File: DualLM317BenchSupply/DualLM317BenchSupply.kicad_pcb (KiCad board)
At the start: 2 copper layers, 39 parts, among them CON101 BARREL_JACK, P103 CONN_1, P104 CONN_1, SW101 SPDT, SW102 SPDT, SW103 SPDT, SW201 SP6T, U101 LM317, U102 LM317, U103 7805

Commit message: updating parts
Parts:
- removed C103, C105: 1uF, C1V7
- removed C104, C107: 10uF, C1V7
- C102: footprint C2V10 -> ELCAP_2_52_V
- CON101: footprint BARREL_JACK -> BARREL_JACK_21x55
- moved U103 14.5 mm to (129.5, 175.3)
- moved C102 9.16 mm to (114.3, 175.3), turned to 270 degrees
- moved CON101 1.27 mm to (101.6, 177.8)
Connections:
- C101 pad 1: N-000009 -> N-0000010
- C102 pad 1: N-000009 -> N-0000010
- C106 pad 1: N-000009 -> N-0000010
- D101 pad 1: N-000009 -> N-0000010
- D104 pad 2: N-000009 -> N-0000010
- SW101 pad 1: N-000009 -> N-0000010
- SW102 pad 2: N-000009 -> N-0000010
- SW201 pad 1: (no net) -> /current_limit_r/IN
- SW201 pad 2: (no net) -> N-0000017
- SW201 pad 3: (no net) -> N-0000016
- SW201 pad 4: (no net) -> N-0000020
- SW201 pad 5: (no net) -> N-0000021
- SW201 pad 6: (no net) -> N-0000018
- SW201 pad 7: (no net) -> N-0000022
- U101 pad 1: N-000009 -> N-0000010
- U103 pad 1: (no net) -> N-0000010
- U103 pad 2: (no net) -> GND
- U103 pad 3: (no net) -> 5V

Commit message: updating switches, capacitors, and LEDs
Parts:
- added C103: 1uF, C1V7, F.Cu at (20.3, 30.5)
- added C104: 10uF, C1V7, F.Cu at (33.0, 30.5)
- added C105: 1uF, C1V7, F.Cu at (43.2, 17.8)
- added C107: 10uF, C1V7, F.Cu at (30.5, 20.3)
- D101: footprint LED-5MM -> LED_5MM
- U101: value LM317 -> 7805
- U103: value 7805 -> LM317
- moved D101 156.2 mm to (121.9, 182.9)
- moved R101 138.5 mm to (129.5, 182.9)
- moved R103 92.4 mm to (207.0, 167.6)
- moved R201 79.3 mm to (168.9, 154.9)
- moved R202 79.3 mm to (193.0, 149.9)
- moved R203 79.3 mm to (175.3, 163.8)
- moved R205 79.3 mm to (193.0, 157.5)
- moved R206 79.3 mm to (179.1, 148.6)
- moved R207 79.3 mm to (154.9, 157.5)
- moved R210 79.3 mm to (189.2, 165.1)
- moved R212 79.3 mm to (160.0, 161.3)
- moved R204 79.3 mm to (156.2, 167.6)
- moved R208 79.3 mm to (184.2, 153.7)
- moved R209 79.3 mm to (174.0, 167.6)
- moved R211 73.9 mm to (185.4, 172.7)
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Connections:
- C101 pad 1: N-0000010 (its old number) -> N-0000015
- C102 pad 1: N-0000010 (its old number) -> N-0000015
- C106 pad 1: N-0000010 (its old number) -> N-0000015
- D101 pad 1: N-0000010 (its old number) -> N-0000015
- D102 pad 1: N-0000015 -> N-000005
- D103 pad 1: N-0000012 (its old number) -> N-0000014
- D103 pad 2: N-0000015 -> N-000005
- D104 pad 2: N-0000010 (its old number) -> N-0000015
- R103 pad 1: N-0000015 -> N-000005
- R103 pad 2: N-0000012 (its old number) -> N-0000014
- RV101 pad 3: N-0000012 (its old number) -> N-0000014
- SW101 pad 1: N-0000010 (its old number) -> N-0000015
- SW102 pad 2: N-0000010 (its old number) -> N-0000015
- SW103 pad 2: N-0000015 -> N-000005
- U101 pad 1: N-0000010 (its old number) -> N-0000015
- U101 pad 2: /current_limit_r/OUT -> GND
- U101 pad 3: /current_limit_r/IN -> 5V
- U102 pad 1: N-0000013 -> /current_limit_r/OUT
- U102 pad 2: N-0000012 (its old number) -> /current_limit_r/IN
- U103 pad 1: N-0000010 (its old number) -> N-0000014
- U103 pad 2: GND -> N-000005
- U103 pad 3: 5V -> N-0000013

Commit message: moving status LED to 5V rail.  starting initial layout.
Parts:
- added D1: 1N4148, D3, F.Cu at (170.2, 188.0)
- C102: value 1000uF -> 100uF
- R101: value 1k -> 150
- R201, R202, R203, R204, R205, R206, R207, R208, R209, R210, R211, R212: footprint R_AXIAL_0W25 -> R1
- moved C105 179.5 mm to (119.4, 180.3)
- moved C103 177.7 mm to (111.8, 182.9)
- moved C107 164.7 mm to (104.1, 167.6)
- moved C104 150.9 mm to (121.9, 152.4)
- moved C106 142.8 mm to (99.1, 154.9)
- moved SW201 141.2 mm to (157.5, 185.4), turned to 180 degrees
- moved C101 140.6 mm to (99.1, 149.9)
- moved SW103 130.3 mm to (127.0, 165.1)
- moved D103 126.2 mm to (109.2, 142.2)
- moved SW101 118.8 mm to (167.6, 157.5), turned to 90 degrees
- moved D104 118.7 mm to (114.3, 124.5)
- moved SW102 112.2 mm to (167.6, 167.6), turned to 90 degrees
- moved D102 106.1 mm to (137.2, 167.6)
- moved RV101 101.8 mm to (167.6, 147.3), turned to 90 degrees
- moved R103 80.0 mm to (127.0, 167.6), turned to 180 degrees
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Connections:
- C101 pad 1: N-0000015 (its old number) -> N-000008
- C102 pad 1: N-0000015 (its old number) -> N-000008
- C104 pad 1: N-0000014 (its old number) -> N-000006
- C106 pad 1: N-0000015 (its old number) -> N-000008
- D101 pad 1: N-0000015 (its old number) -> 5V
- D103 pad 1: N-0000014 (its old number) -> N-000006
- D104 pad 2: N-0000015 (its old number) -> N-000008
- R103 pad 2: N-0000014 (its old number) -> N-000006
- RV101 pad 2: GND -> N-000006
- RV101 pad 3: N-0000014 (its old number) -> N-000006
- SW101 pad 1: N-0000015 (its old number) -> N-000008
- SW102 pad 2: N-0000015 (its old number) -> N-000008
- U101 pad 1: N-0000015 (its old number) -> N-000008
- U102 pad 3: N-0000015 (its old number) -> N-000008
- U103 pad 1: N-0000014 (its old number) -> N-000006
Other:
- board outline added: 81.3 x 68.6 mm

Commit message: working on board layout
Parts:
- removed C101, C106: 0.1uF, C2
- removed C102: 100uF, ELCAP_2_52_V
- removed C103, C105: 1uF, C1V7
- removed C104, C107: 10uF, C1V7
- removed CON101: BARREL_JACK, BARREL_JACK_21x55
- removed D1, D102, D103, D104: 1N4148, D3
- removed D101: LED, LED_5MM
- removed DS101: AMMETER, PIN_ARRAY_4x1
- removed DS102: VOLTMETER, PIN_ARRAY_3X1
- removed the H*** at (124.5, 133.3)
- removed P103, P104: CONN_1, PIN_ARRAY_1
- removed R101: 150, R_AXIAL_0W25
- removed R103: 330, R_AXIAL_0W25
- removed RV101: 5k, PIN_ARRAY_3X1
- removed SW101, SW102, SW103: SPDT, PIN_ARRAY_3X1
- removed U101: 7805, TO-220_V_069B
- removed U102, U103: LM317, TO-220_V_069B
- added H***: Val**, hole_M3, F.Cu at (139.7, 261.6)
- added H***: Val**, hole_M3, F.Cu at (233.0, 261.6)
- SW201: footprint pin_array_8x2 -> G3SR022-R
- moved R207 99.0 mm to (171.4, 257.2), turned to 0 degrees
- moved R206 94.0 mm to (171.4, 253.4), turned to 0 degrees
- moved R210 90.9 mm to (168.9, 240.7), turned to 90 degrees
- moved R203 88.4 mm to (147.3, 233.0), turned to 90 degrees
- moved R202 86.2 mm to (143.5, 235.6), turned to 90 degrees
- moved R205 85.4 mm to (171.4, 249.6), turned to 0 degrees
- moved R212 84.2 mm to (161.3, 235.6)
- moved R209 83.8 mm to (165.1, 239.4), turned to 90 degrees
- moved R211 79.3 mm to (156.2, 233.0)
- moved R201 76.9 mm to (139.7, 239.4)
- moved R204 70.6 mm to (171.4, 245.7), turned to 0 degrees
- moved R208 60.5 mm to (152.4, 233.0)
- moved SW201 59.1 mm to (154.9, 244.5), turned to 0 degrees
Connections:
- R204 pad 1: N-0000019 -> N-0000015
- R204 pad 2: N-0000018 -> /current_limit_r/OUT
- R205 pad 1: N-0000018 -> N-0000015
- R206 pad 1: N-0000020 -> N-0000015
- R207 pad 1: N-0000017 (its old number) -> N-0000015
- R208 pad 1: N-0000017 (its old number) -> N-0000020
- R208 pad 2: /current_limit_r/OUT -> N-0000016
- R209 pad 1: N-0000021 (its old number) -> N-0000019
- R210 pad 1: N-0000021 (its old number) -> N-0000019
- R211 pad 1: N-0000021 (its old number) -> N-0000016
- R212 pad 1: N-0000021 (its old number) -> N-0000018
- SW201 pad 4: N-0000019 -> N-0000020
- SW201 pad 5: N-0000020 -> N-0000018
- SW201 pad 6: N-0000017 (its old number) -> N-0000019
- SW201 pad 7: N-0000021 (its old number) -> N-0000015
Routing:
- net N-0000015: track 0.00 -> 42.6 mm
- net N-0000019: track 0.00 -> 39.8 mm
- net /current_limit_r/OUT: track 0.00 -> 20.6 mm
- net /current_limit_r/IN: track 0.00 -> 11.6 mm
- net N-0000017: track 0.00 -> 10.3 mm
- net N-0000020: track 0.00 -> 6.13 mm
- net N-0000018: track 0.00 -> 6.03 mm
- net N-0000021: track 0.00 -> 6.02 mm
- net N-0000016: track 0.00 -> 4.86 mm
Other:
- board size 81.3 x 68.6 mm -> 99.7 x 149.9 mm

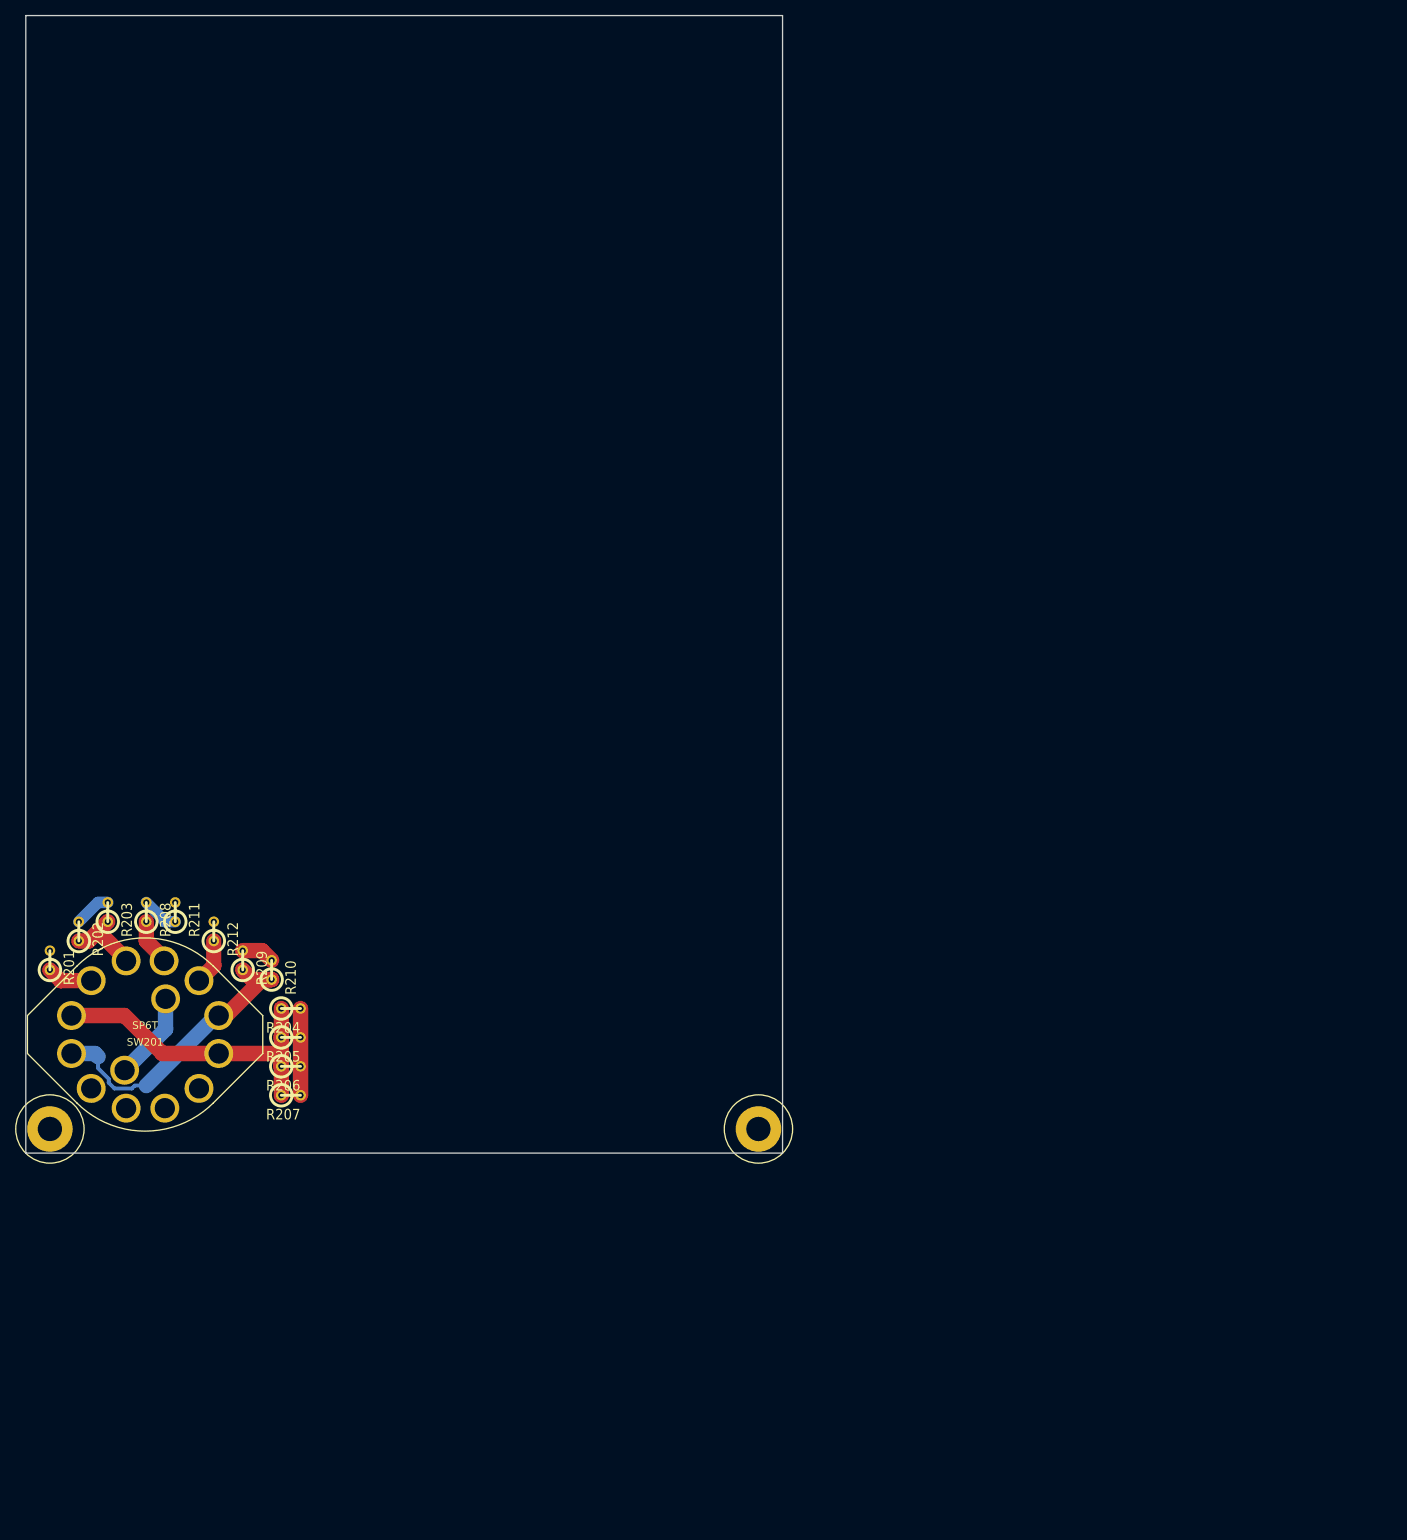
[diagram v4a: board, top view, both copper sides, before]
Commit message: working on layout of current limit selector switch resistors.
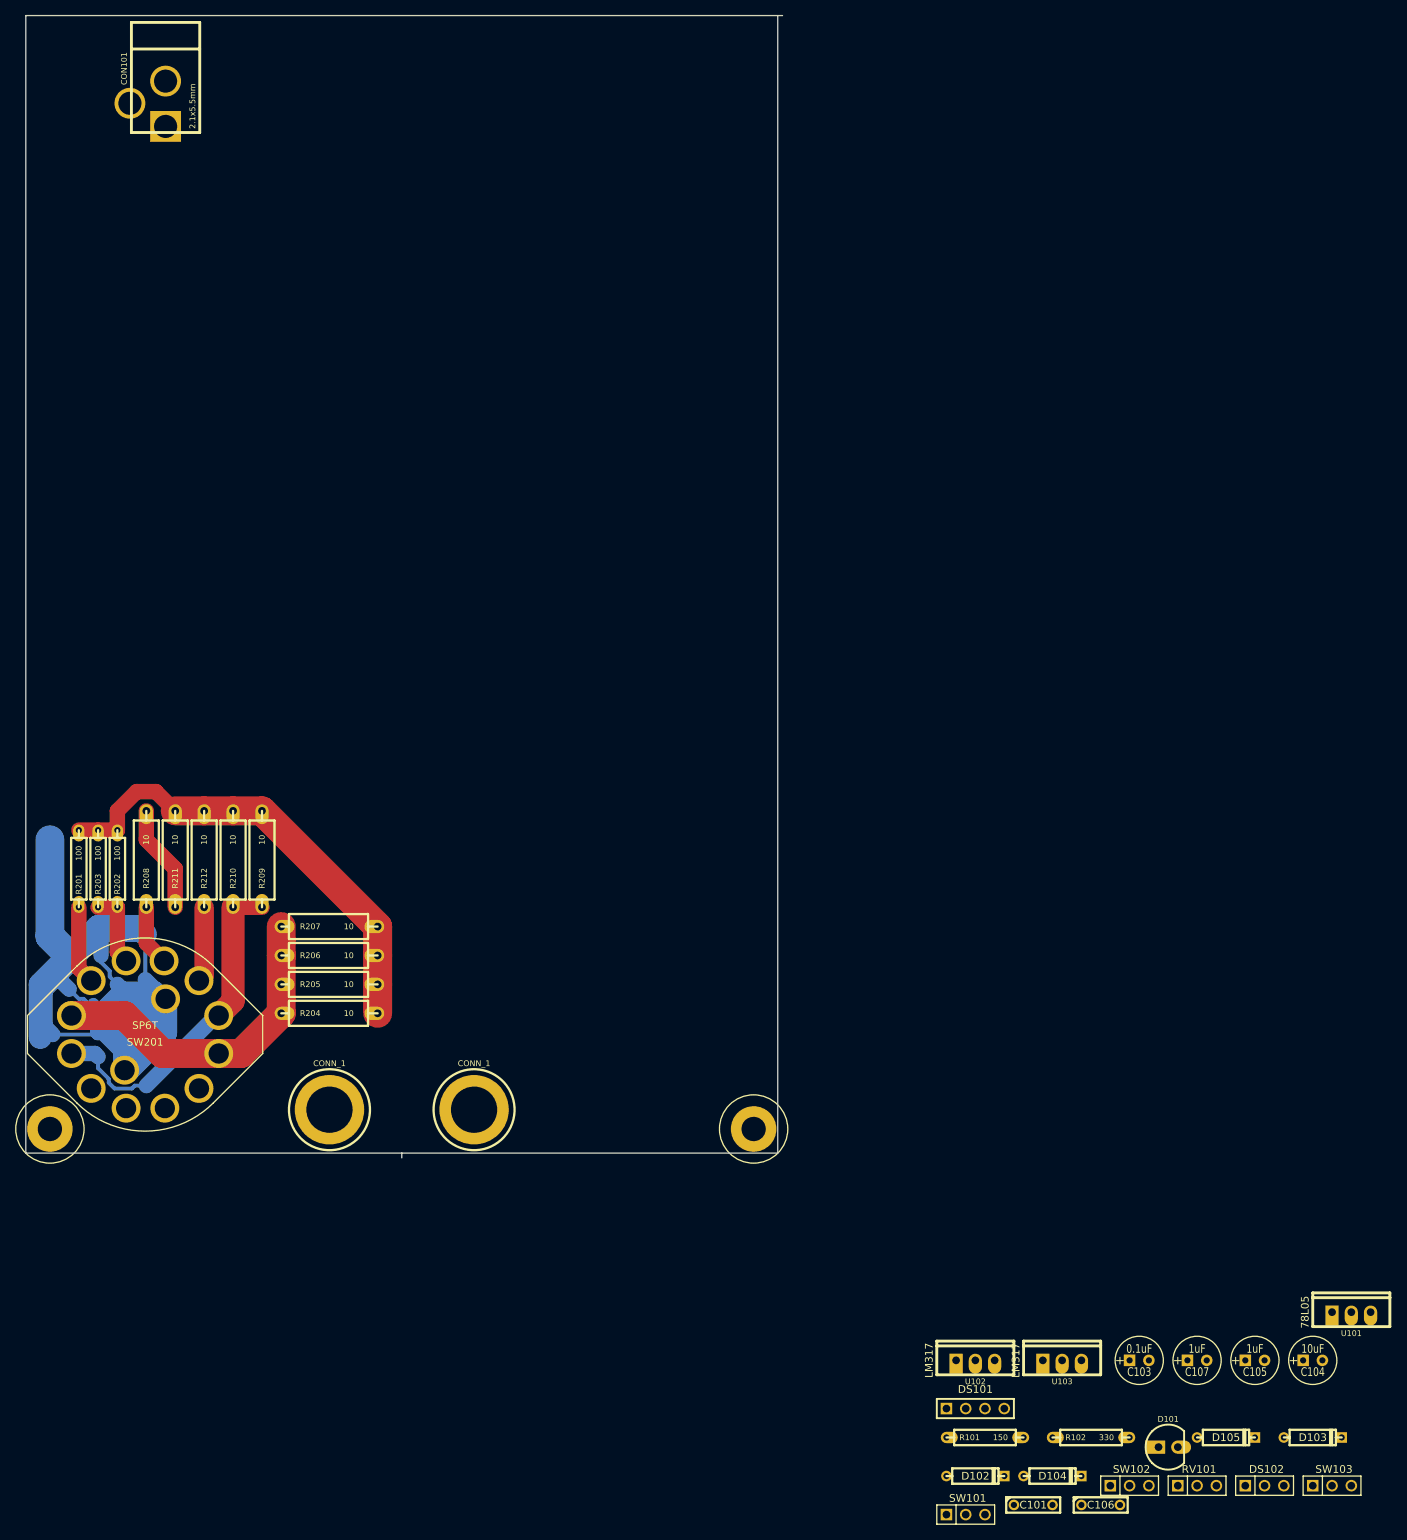
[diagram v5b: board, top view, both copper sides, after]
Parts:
- added C101: 100uF, C2, F.Cu at (269.2, 311.1)
- added C103: 0.1uF, C1V7, F.Cu at (283.2, 292.1)
- added C104: 10uF, C1V7, F.Cu at (306.1, 292.1)
- added C105: 1uF, C1V7, F.Cu at (298.4, 292.1)
- added C106: 10uF, C2, F.Cu at (278.1, 311.1)
- added C107: 1uF, C1V7, F.Cu at (290.8, 292.1)
- added CON101: BARREL_JACK, BARREL_JACK_21x55, F.Cu at (154.9, 129.5)
- added D101: 1N4148, LED_5MM, F.Cu at (285.8, 303.5)
- added D102: 1N4148, D3, F.Cu at (261.6, 307.3)
- added D103: LED, D3, F.Cu at (306.1, 302.3)
- added D104: 1N4148, D3, F.Cu at (271.8, 307.3)
- added D105: 1N4148, D3, F.Cu at (294.6, 302.3)
- added DS101: VOLTMETER, PIN_ARRAY_4x1, F.Cu at (261.6, 298.4)
- added DS102: AMMETER_V, PIN_ARRAY_3X1, F.Cu at (299.7, 308.6)
- added P101: CONN_1, Banana_A, F.Cu at (195.6, 259.1)
- added P102: CONN_1, Banana_A, F.Cu at (176.5, 259.1)
- added R101: 150, R_AXIAL_0W25, F.Cu at (257.8, 302.3)
- added R102: 330, R_AXIAL_0W25, F.Cu at (271.8, 302.3)
- added RV101: 4k7, PIN_ARRAY_3X1, F.Cu at (290.8, 308.6)
- added SW101: SPDT, PIN_ARRAY_3X1, F.Cu at (260.4, 312.4)
- added SW102: SPDT, PIN_ARRAY_3X1, F.Cu at (281.9, 308.6)
- added SW103: SPDT, PIN_ARRAY_3X1, F.Cu at (308.6, 308.6)
- added U101: 78L05, TO-220_V_069B, F.Cu at (308.6, 285.8)
- added U102: LM317, TO-220_V_069B, F.Cu at (259.1, 292.1)
- added U103: LM317, TO-220_V_069B, F.Cu at (270.5, 292.1)
- R201, R202, R203: footprint R1 -> R_AXIAL_0W25
- R204, R205, R206, R207, R208, R209, R210, R211, R212: footprint R1 -> R_AXIAL_0W5
- moved R207 22.3 mm to (170.2, 234.9)
- moved R206 14.7 mm to (170.2, 238.8)
- moved R210 9.69 mm to (163.8, 232.4)
- moved R201 7.96 mm to (143.5, 232.4)
- moved R209 7.43 mm to (167.6, 232.4)
- moved R205 7.10 mm to (170.2, 242.6)
- moved R202 5.99 mm to (148.6, 232.4)
- moved R212 3.42 mm to (160.0, 232.4)
- moved R203 1.42 mm to (146.1, 232.4)
- moved R204 1.42 mm to (170.2, 246.4)
- moved H*** 0.63 mm to (232.4, 261.6)
- moved R208 0.63 mm to (152.4, 232.4)
- moved R211 0.63 mm to (156.2, 232.4)
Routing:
- net /current_limit_r/IN: track 11.6 -> 181.5 mm
- net /current_limit_r/OUT: track 20.6 -> 61.8 mm
- net N-0000016: track 4.86 -> 14.3 mm
- net N-0000019: track 39.8 -> 45.3 mm
- net N-0000021: track 6.02 -> 10.3 mm
- net N-0000018: track 6.03 -> 9.95 mm
- net N-0000020: track 6.13 -> 8.03 mm
- net N-0000015: track 42.6 -> 43.3 mm
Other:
- board size 99.7 x 149.9 mm -> 99.7 x 150.5 mm
